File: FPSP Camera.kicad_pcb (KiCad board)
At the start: 4 copper layers, 85.7 x 35 mm, 61 parts, among them J101 Conn_01x24_Socket, U103 RP2350_60QFN, U104 TLV75533PDRV, U105 TLV73328PDRV, U106 TLV73315PDRV, Y101 SiT8008xx-1x-xxE

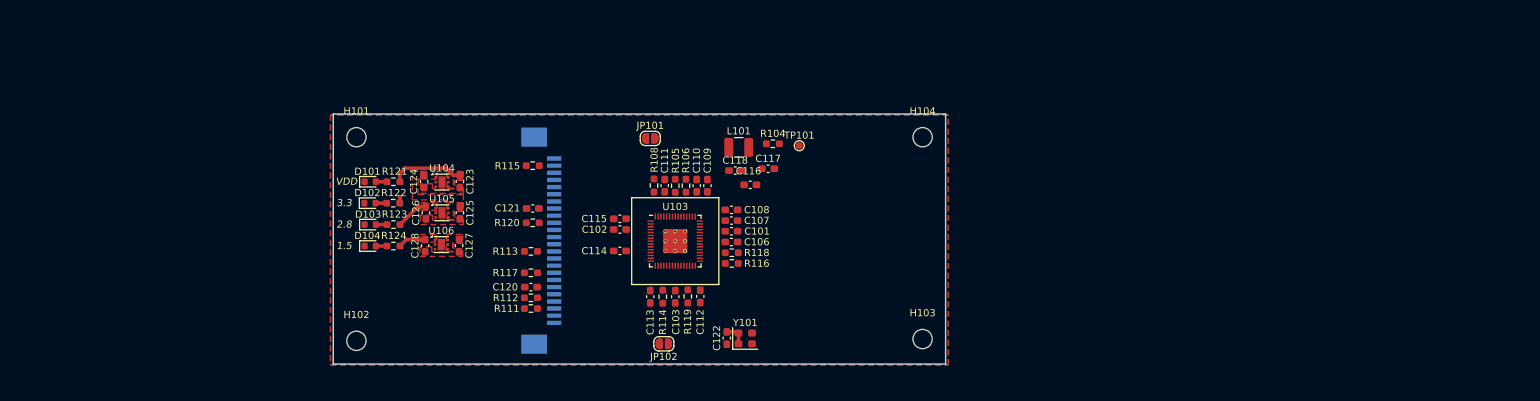
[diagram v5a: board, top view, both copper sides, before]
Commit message: update MCU layout (initial draft)
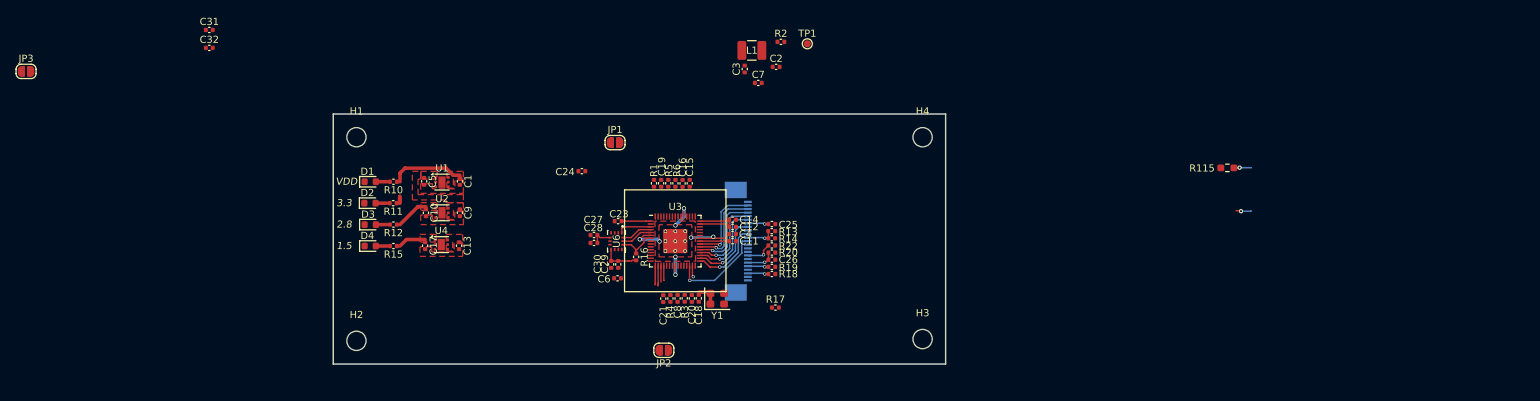
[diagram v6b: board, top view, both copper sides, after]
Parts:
- removed J101: Conn_01x24_Socket, Connector_FFC-FPC:TE_2-84952-4_1x24-1MP_P1.0mm_Horizontal
- added C27: 0.1u, Capacitor_SMD:C_0402_1005Metric, F.Cu at (55.5, 29.5)
- added C28: 0.1u, Capacitor_SMD:C_0402_1005Metric, F.Cu at (55.5, 30.6)
- added C29: 0.1u, Capacitor_SMD:C_0402_1005Metric, F.Cu at (58.9, 33.6)
- added C30: 0.1u, Capacitor_SMD:C_0402_1005Metric, F.Cu at (57.9, 33.6)
- added C31: 0.1u, Capacitor_SMD:C_0402_1005Metric, F.Cu at (1.68, 0.76)
- added C32: 0.1u, Capacitor_SMD:C_0402_1005Metric, F.Cu at (1.68, 3.27)
- added J4: Conn_01x24_Socket, Connector_FFC-FPC:TE_2-1734839-3_1x23-1MP_P0.5mm_Horizontal, B.Cu at (75.7, 30.3)
- added JP3: SolderJumper_2_Open, Jumper:SolderJumper-2_P1.3mm_Open_RoundedPad1.0x1.5mm, F.Cu at (-24.0, 6.55)
- added R16: 10k, Capacitor_SMD:C_0402_1005Metric, F.Cu at (61.4, 32.5)
- added U6: ICM-45686, ICM_45686:IC_ICM-45686, F.Cu at (58.7, 30.3)
- C1: renamed from C123; footprint Capacitor_SMD:C_0603_1608Metric_Pad1.08x0.95mm_HandSolder -> Capacitor_SMD:C_0402_1005Metric
- C10: renamed from C126; footprint Capacitor_SMD:C_0603_1608Metric_Pad1.08x0.95mm_HandSolder -> Capacitor_SMD:C_0402_1005Metric
- C11: renamed from C106; footprint Capacitor_SMD:C_0603_1608Metric_Pad1.08x0.95mm_HandSolder -> Capacitor_SMD:C_0402_1005Metric
- C12: renamed from C107; footprint Capacitor_SMD:C_0603_1608Metric_Pad1.08x0.95mm_HandSolder -> Capacitor_SMD:C_0402_1005Metric
- C13: renamed from C127; footprint Capacitor_SMD:C_0603_1608Metric_Pad1.08x0.95mm_HandSolder -> Capacitor_SMD:C_0402_1005Metric
- C14: renamed from C108; footprint Capacitor_SMD:C_0603_1608Metric_Pad1.08x0.95mm_HandSolder -> Capacitor_SMD:C_0402_1005Metric
- C15: renamed from C109; footprint Capacitor_SMD:C_0603_1608Metric_Pad1.08x0.95mm_HandSolder -> Capacitor_SMD:C_0402_1005Metric
- C16: renamed from C110; footprint Capacitor_SMD:C_0603_1608Metric_Pad1.08x0.95mm_HandSolder -> Capacitor_SMD:C_0402_1005Metric
- C17: renamed from C128; footprint Capacitor_SMD:C_0603_1608Metric_Pad1.08x0.95mm_HandSolder -> Capacitor_SMD:C_0402_1005Metric
- C18: renamed from C122; footprint Capacitor_SMD:C_0603_1608Metric_Pad1.08x0.95mm_HandSolder -> Capacitor_SMD:C_0402_1005Metric
- C19: renamed from C111; footprint Capacitor_SMD:C_0603_1608Metric_Pad1.08x0.95mm_HandSolder -> Capacitor_SMD:C_0402_1005Metric
- C2: renamed from C117; footprint Capacitor_SMD:C_0603_1608Metric_Pad1.08x0.95mm_HandSolder -> Capacitor_SMD:C_0402_1005Metric
- C20: renamed from C112; footprint Capacitor_SMD:C_0603_1608Metric_Pad1.08x0.95mm_HandSolder -> Capacitor_SMD:C_0402_1005Metric
- C21: renamed from C113; footprint Capacitor_SMD:C_0603_1608Metric_Pad1.08x0.95mm_HandSolder -> Capacitor_SMD:C_0402_1005Metric
- C23: renamed from C114; footprint Capacitor_SMD:C_0603_1608Metric_Pad1.08x0.95mm_HandSolder -> Capacitor_SMD:C_0402_1005Metric
- C24: renamed from C115; footprint Capacitor_SMD:C_0603_1608Metric_Pad1.08x0.95mm_HandSolder -> Capacitor_SMD:C_0402_1005Metric
- C25: renamed from C121; footprint Capacitor_SMD:C_0603_1608Metric_Pad1.08x0.95mm_HandSolder -> Capacitor_SMD:C_0402_1005Metric
- C26: renamed from C120; footprint Capacitor_SMD:C_0603_1608Metric_Pad1.08x0.95mm_HandSolder -> Capacitor_SMD:C_0402_1005Metric
- C3: renamed from C118; footprint Capacitor_SMD:C_0603_1608Metric_Pad1.08x0.95mm_HandSolder -> Capacitor_SMD:C_0402_1005Metric
- C4: renamed from C101; footprint Capacitor_SMD:C_0603_1608Metric_Pad1.08x0.95mm_HandSolder -> Capacitor_SMD:C_0402_1005Metric
- C5: renamed from C124; footprint Capacitor_SMD:C_0603_1608Metric_Pad1.08x0.95mm_HandSolder -> Capacitor_SMD:C_0402_1005Metric
- C6: renamed from C102; footprint Capacitor_SMD:C_0603_1608Metric_Pad1.08x0.95mm_HandSolder -> Capacitor_SMD:C_0402_1005Metric
- C7: renamed from C116; footprint Capacitor_SMD:C_0603_1608Metric_Pad1.08x0.95mm_HandSolder -> Capacitor_SMD:C_0402_1005Metric
- C8: renamed from C103; footprint Capacitor_SMD:C_0603_1608Metric_Pad1.08x0.95mm_HandSolder -> Capacitor_SMD:C_0402_1005Metric
- C9: renamed from C125; footprint Capacitor_SMD:C_0603_1608Metric_Pad1.08x0.95mm_HandSolder -> Capacitor_SMD:C_0402_1005Metric
- R1: renamed from R108; footprint Resistor_SMD:R_0603_1608Metric_Pad0.98x0.95mm_HandSolder -> Capacitor_SMD:C_0402_1005Metric
- R10: renamed from R121; footprint Resistor_SMD:R_0603_1608Metric_Pad0.98x0.95mm_HandSolder -> Capacitor_SMD:C_0402_1005Metric
- R11: renamed from R122; footprint Resistor_SMD:R_0603_1608Metric_Pad0.98x0.95mm_HandSolder -> Capacitor_SMD:C_0402_1005Metric
- R12: renamed from R123; footprint Resistor_SMD:R_0603_1608Metric_Pad0.98x0.95mm_HandSolder -> Capacitor_SMD:C_0402_1005Metric
- R13: renamed from R116; footprint Resistor_SMD:R_0603_1608Metric_Pad0.98x0.95mm_HandSolder -> Capacitor_SMD:C_0402_1005Metric
- R14: renamed from R118; footprint Resistor_SMD:R_0603_1608Metric_Pad0.98x0.95mm_HandSolder -> Capacitor_SMD:C_0402_1005Metric
- R15: renamed from R124; footprint Resistor_SMD:R_0603_1608Metric_Pad0.98x0.95mm_HandSolder -> Capacitor_SMD:C_0402_1005Metric
- R17: renamed from R120; footprint Resistor_SMD:R_0603_1608Metric_Pad0.98x0.95mm_HandSolder -> Capacitor_SMD:C_0402_1005Metric
- R18: renamed from R111; footprint Resistor_SMD:R_0603_1608Metric_Pad0.98x0.95mm_HandSolder -> Capacitor_SMD:C_0402_1005Metric
- R19: renamed from R112; footprint Resistor_SMD:R_0603_1608Metric_Pad0.98x0.95mm_HandSolder -> Capacitor_SMD:C_0402_1005Metric
- R2: renamed from R104; footprint Resistor_SMD:R_0603_1608Metric_Pad0.98x0.95mm_HandSolder -> Capacitor_SMD:C_0402_1005Metric
- R20: renamed from R113; footprint Resistor_SMD:R_0603_1608Metric_Pad0.98x0.95mm_HandSolder -> Capacitor_SMD:C_0402_1005Metric
- R22: renamed from R117; footprint Resistor_SMD:R_0603_1608Metric_Pad0.98x0.95mm_HandSolder -> Capacitor_SMD:C_0402_1005Metric
- R3: renamed from R119; footprint Resistor_SMD:R_0603_1608Metric_Pad0.98x0.95mm_HandSolder -> Capacitor_SMD:C_0402_1005Metric
- R4: renamed from R114; footprint Resistor_SMD:R_0603_1608Metric_Pad0.98x0.95mm_HandSolder -> Capacitor_SMD:C_0402_1005Metric
- R5: renamed from R105; footprint Resistor_SMD:R_0603_1608Metric_Pad0.98x0.95mm_HandSolder -> Capacitor_SMD:C_0402_1005Metric
- R6: renamed from R106; footprint Resistor_SMD:R_0603_1608Metric_Pad0.98x0.95mm_HandSolder -> Capacitor_SMD:C_0402_1005Metric
- moved R115 97.2 mm to (144.2, 20.1)
- moved R17 36.0 mm to (80.9, 39.6)
- moved R18 34.1 mm to (80.4, 34.9), turned to 180 degrees
- moved R19 34.0 mm to (80.4, 33.9), turned to 180 degrees
- moved C26 33.9 mm to (80.4, 32.9), turned to 0 degrees
- moved R22 33.9 mm to (80.4, 30.9), turned to 0 degrees
- moved R20 33.7 mm to (80.4, 31.9), turned to 180 degrees
- moved C25 33.5 mm to (80.4, 27.9), turned to 0 degrees
- moved C2 14.3 mm to (81.0, 5.92)
- moved C7 14.3 mm to (78.5, 8.17)
- moved R2 14.3 mm to (81.7, 2.42)
- moved TP1 14.3 mm to (85.4, 2.69)
- moved C3 14.3 mm to (76.6, 6.22), turned to 90 degrees
- moved L1 13.7 mm to (77.6, 3.62), turned to 180 degrees
- moved C24 8.54 mm to (53.8, 20.5)
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- renumbered D101 to D1, D102 to D2, D103 to D3, D104 to D4, H101 to H1, H102 to H2, H103 to H3, H104 to H4, JP101 to JP1, JP102 to JP2, L101 to L1, TP101 to TP1, U104 to U1, U105 to U2, U103 to U3, U106 to U4, Y101 to Y1
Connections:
- U3 pad 10: VSYNC_1 -> unconnected-(U3-GPIO7-Pad10)
- U3 pad 12: SDA_cam_1 -> unconnected-(U3-GPIO8-Pad12)
- U3 pad 13: SCL_cam_1 -> unconnected-(U3-GPIO9-Pad13)
- U3 pad 14: ~{RESET_1} -> unconnected-(U3-GPIO10-Pad14)
- U3 pad 15: DATA8_1 -> unconnected-(U3-GPIO11-Pad15)
- U3 pad 16: DATA7_1 -> IMAGE_OUT_1_1+
- U3 pad 17: PCLK_1 -> IMAGE_OUT_1_1-
- U3 pad 18: DATA6_1 -> IMAGE_OUT_2_1+
- U3 pad 19: DATA2_1 -> IMAGE_OUT_2_1-
- U3 pad 27: DATA5_1 -> POSITION_OUT_1
- U3 pad 28: DATA3_1 -> DATA9_1
- U3 pad 29: DATA4_1 -> EXT_XCLK_1
- U3 pad 3: CS_1 -> /IMU_SDO
- U3 pad 31: DATA9_1 -> DATA8_1
- U3 pad 32: EXT_XCLK_1 -> DATA7_1
- U3 pad 33: HSYNC_1 -> DATA6_1
- U3 pad 34: INT_XCLK -> DATA2_1
- U3 pad 35: IMAGE_OUT_1_1 -> DATA5_1
- U3 pad 36: IMAGE_OUT_2_1 -> DATA3_1
- U3 pad 37: POSITION_OUT_1 -> DATA4_1
- U3 pad 4: SDO_imu_1 -> /IMU_SDI
- U3 pad 5: SDA_imu_1 -> /IMU_SCLK
- U3 pad 7: SCL_imu_1 -> /~{IMU_CS}
- U3 pad 8: INT1_1 -> unconnected-(U3-GPIO5-Pad8)
- U3 pad 9: INT2_1 -> unconnected-(U3-GPIO6-Pad9)
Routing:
- net +1V1: track 0.00 -> 20.2 mm, vias 0 -> 8
- net +3.3V: track 5.07 -> 22.7 mm
- net DATA9_1: track 0.00 -> 13.5 mm, vias 0 -> 1
- net DATA3_1: track 0.00 -> 11.9 mm, vias 0 -> 1
- net DATA5_1: track 0.00 -> 11.7 mm, vias 0 -> 1
- net DATA4_1: track 0.00 -> 11.7 mm, vias 0 -> 1
- net DATA2_1: track 0.00 -> 11.6 mm, vias 0 -> 1
- net DATA6_1: track 0.00 -> 11.5 mm, vias 0 -> 1
- net DATA7_1: track 0.00 -> 10.8 mm, vias 0 -> 1
- net DATA8_1: track 0.00 -> 10.2 mm, vias 0 -> 1
- net +3V3: track 0.00 -> 8.29 mm
- net /~{IMU_CS}: track 0.00 -> 6.05 mm
- net PCLK_1: track 0.00 -> 5.11 mm, vias 0 -> 2
- net /IMU_SDO: track 0.00 -> 4.76 mm
- net /IMU_SCLK: track 0.00 -> 4.38 mm
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- added copper zone on F.Cu, net +1V1
- removed copper zone on B.Cu, net (none)
- removed copper zone on F.Cu, net (none)
